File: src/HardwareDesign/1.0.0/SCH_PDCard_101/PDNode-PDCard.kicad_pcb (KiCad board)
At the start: 6 copper layers, 53.9 x 35.5 mm, 132 parts, among them IC1 TPS552882QRPMRQ1, IC2 MCP22350T-2I/Q8X, IC3 INA219BIDCNT, IC4 SN74LVC1G97QDCKRQ1, IC5 SN74LVC1G97QDCKRQ1, IC6 TPS74801DRCT, IC7 SN74LVC1G97QDCKRQ1, J1 USB_C_Receptacle_PowerOnly_6P, J2 PCIE EDGE CONNECTOR, T1 BSZ065N06, T2 BSZ065N06, T3 DMP3013SFV, T4 DMP3013SFV, T5 DMP3013SFV, U1 24AA02E-OT

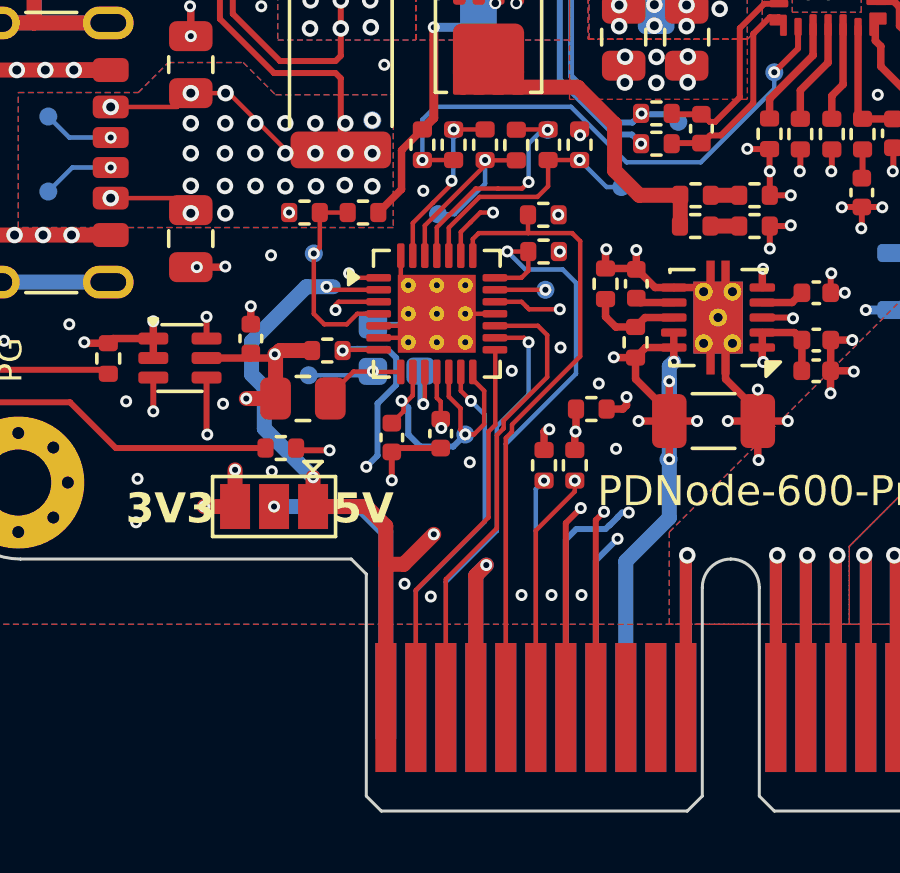
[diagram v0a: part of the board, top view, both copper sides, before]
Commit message: Add bladecore to design
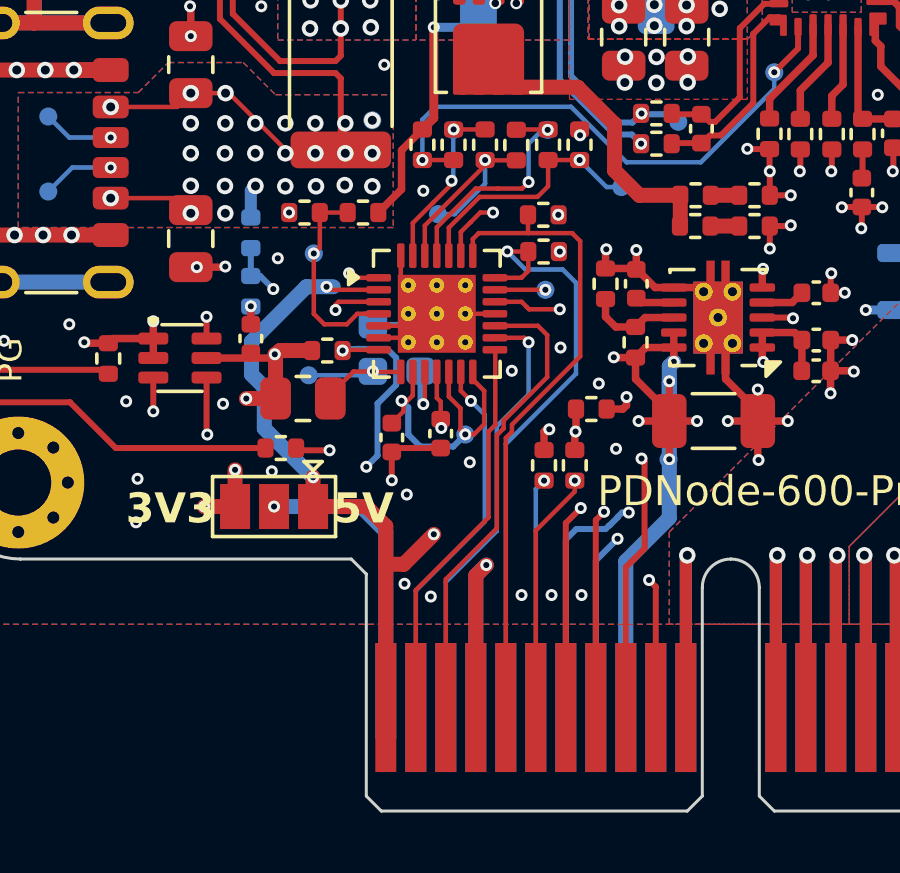
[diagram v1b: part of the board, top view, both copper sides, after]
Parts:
- added R52: 90.9K 1%, Resistor_SMD:R_0402_1005Metric, B.Cu at (153.8, 79.2)
- added R53: 10K 1%, Resistor_SMD:R_0402_1005Metric, B.Cu at (153.8, 81.1)
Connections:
- net PGOOD_COMBIMED renamed PGOOD_COMBINED
- J2 pad B10: unconnected-(J2-PadB10) -> /Block Diagram/Board Connector and Supplies/VBUS_VMON_PORT0
- J2 pad B9: unconnected-(J2-PadB9) -> /Block Diagram/USB-PD Source Controller/VBUS_DET
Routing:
- net /Block Diagram/Board Connector and Supplies/VBUS_VMON_PORT0: track 0.00 -> 26.4 mm, vias 0 -> 3
- net /Block Diagram/USB-PD Source Controller/VBUS_DET: track 6.84 -> 31.6 mm, vias 1 -> 2
- net VBUS: track 20.2 -> 21.3 mm
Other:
- board text added: "LAYER STACKUP ==================================== Top F.Silkscreen Top silkscreen (White, Direct Printing) F.Paste Top paste F.Mask Top mask (Green, 0.02mm, Solder Resist, Er=3.8) L1 (Sig,PWR) Copper 0.035mm Dielectric 1 Prepreg 1/1 FR4 natural 0.0994mm 3313 RC57% 4.2mil, Er=4.1, LossTg=0.02 L2 (GND) Copper 0.0152mm Dielectric 2 Core 1/1 FR4 natural 0.55mm 0.55mm H/Hwithout copper, Er=4.41, Loss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"
- board text added: "PCB AREA"
